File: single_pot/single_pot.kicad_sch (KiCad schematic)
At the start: 4 parts, among them J1 I/O connector

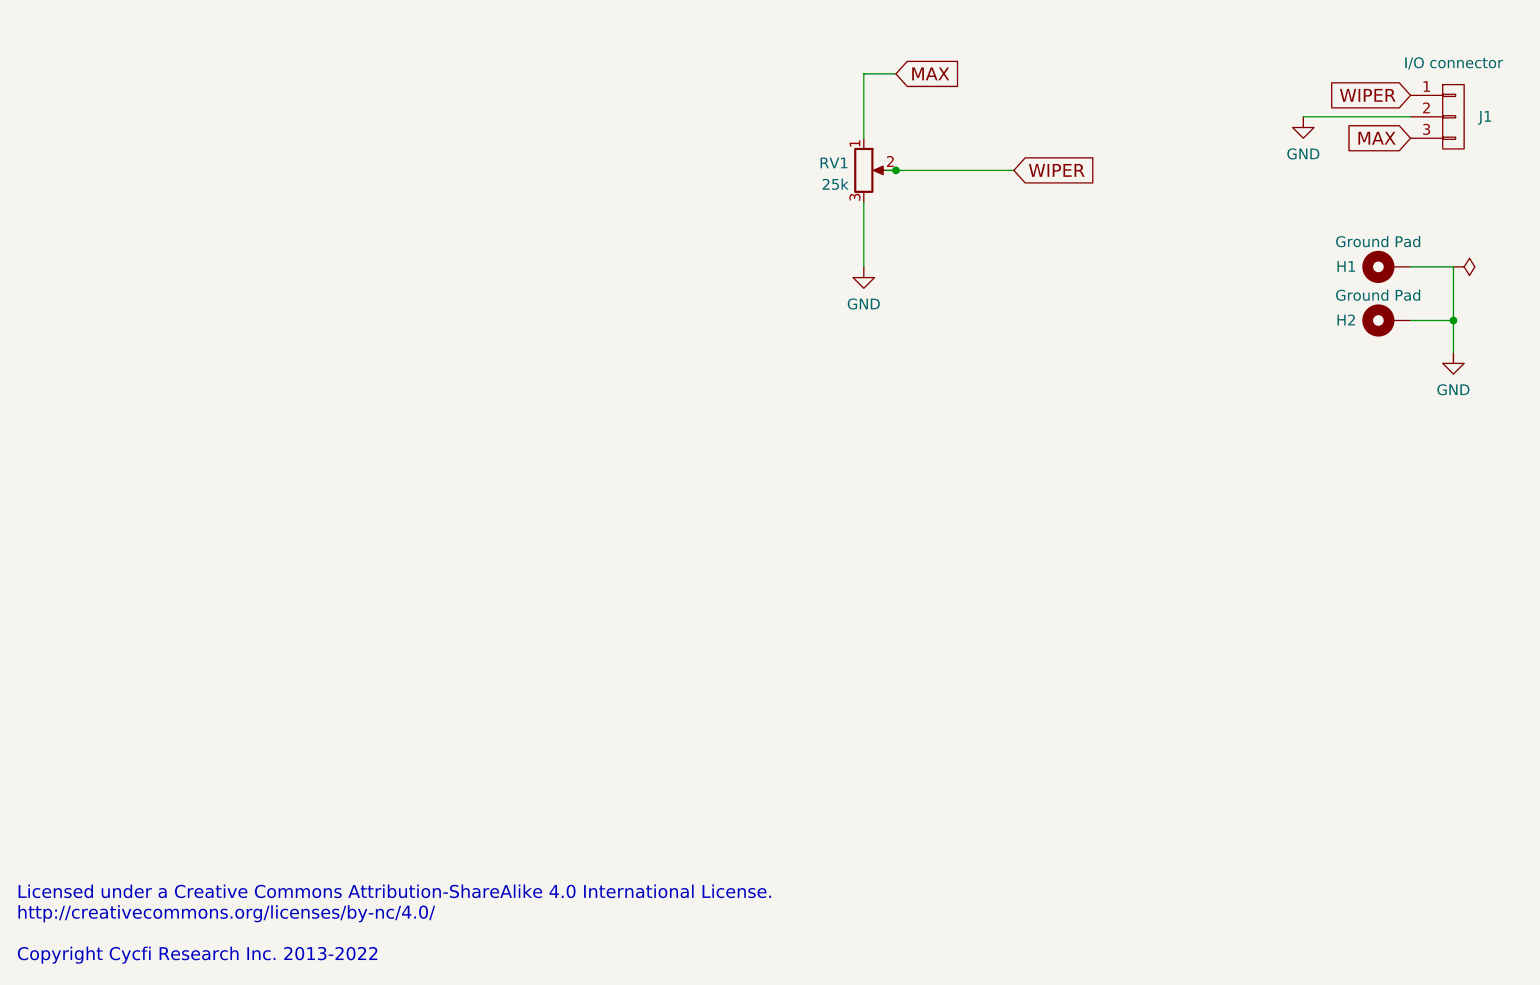
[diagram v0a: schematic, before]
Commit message: Added taper resistor
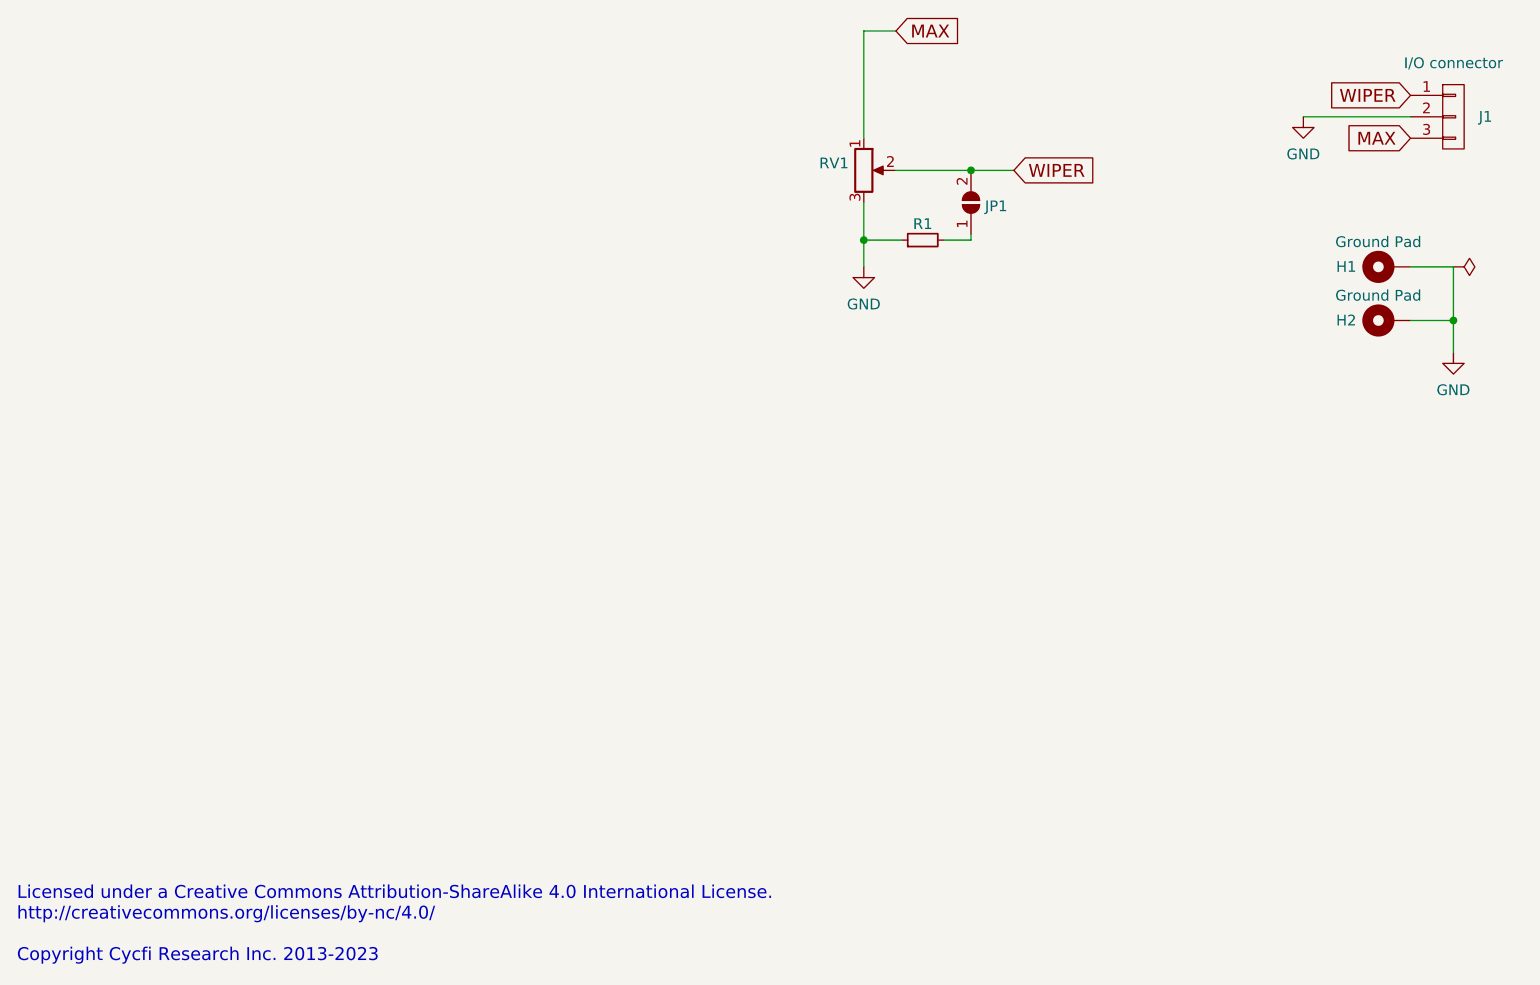
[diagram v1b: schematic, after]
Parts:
- added JP1: SolderJumper_2_Open, Jumper:SolderJumper-2_P1.3mm_Open_TrianglePad1.0x1.5mm, symbol Jumper:SolderJumper_2_Open
- added R1: 4.7k, Resistor_SMD:R_0805_2012Metric_Pad1.20x1.40mm_HandSolder, symbol Device:R_Small
- RV1: value 25k -> 500k
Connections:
- net GND: now also R1.1
- net WIPER: now also JP1.2 (B)
- new net: JP1.1 (A), R1.2
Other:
- note added: "Licensed under a Creative Commons Attribution-ShareAlike 4.0 International License. http://creativecommons.org/licenses/by-nc/4.0/ Copyright Cycfi Research Inc. 2013-2023"
- note removed: "Licensed under a Creative Commons Attribution-ShareAlike 4.0 International License. http://creativecommons.org/licenses/by-nc/4.0/ Copyright Cycfi Research Inc. 2013-2022"
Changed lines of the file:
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@@
   (title_block
     (title "CV Pot Big")
-    (date "2022-04-20")
-    (rev "v3.0")
+    (date "2023-08-05")
+    (rev "v3.1")
     (company "Document Number: 2022005")
   )
   (junction (at 194.31 111.76) (diameter 0) (color 0 0 0 0)
   )
-  (junction (at 128.27 93.98) (diameter 0) (color 0 0 0 0)
+  (junction (at 137.16 93.98) (diameter 0) (color 0 0 0 0)
+  )
+  (junction (at 124.46 102.235) (diameter 0) (color 0 0 0 0)
   )
   (wire (pts (xy 189.23 105.41) (xy 194.31 105.41))
@@
     (stroke (width 0) (type default) (color 0 0 0 0))
   )
-  (wire (pts (xy 124.46 97.79) (xy 124.46 105.41))
-    (stroke (width 0) (type default) (color 0 0 0 0))
-  )
-  (wire (pts (xy 128.27 82.55) (xy 124.46 82.55))
+  (wire (pts (xy 124.46 97.79) (xy 124.46 102.235))
+    (stroke (width 0) (type default) (color 0 0 0 0))
+  )
+  (wire (pts (xy 137.16 102.235) (xy 133.985 102.235))
+    (stroke (width 0) (type default) (color 0 0 0 0))
+  )
+  (wire (pts (xy 137.16 93.98) (xy 142.24 93.98))
+    (stroke (width 0) (type default) (color 0 0 0 0))
+  )
+  (wire (pts (xy 128.27 77.47) (xy 124.46 77.47))
+    (stroke (width 0) (type default) (color 0 0 0 0))
+  )
+  (wire (pts (xy 137.16 101.6) (xy 137.16 102.235))
     (stroke (width 0) (type default) (color 0 0 0 0))
   )
@@
     (stroke (width 0) (type default) (color 0 0 0 0))
   )
-  (wire (pts (xy 128.27 93.98) (xy 142.24 93.98))
-    (stroke (width 0) (type default) (color 0 0 0 0))
-  )
-  (wire (pts (xy 124.46 82.55) (xy 124.46 90.17))
+  (wire (pts (xy 124.46 77.47) (xy 124.46 90.17))
+    (stroke (width 0) (type default) (color 0 0 0 0))
+  )
+  (wire (pts (xy 128.27 93.98) (xy 137.16 93.98))
     (stroke (width 0) (type default) (color 0 0 0 0))
   )
@@
     (stroke (width 0) (type default) (color 0 0 0 0))
   )
-  (wire (pts (xy 127 93.98) (xy 128.27 93.98))
-    (stroke (width 0) (type default) (color 0 0 0 0))
-  )
-  (text "Licensed under a Creative Commons Attribution-ShareAlike 4.0 International License. \nhttp://creativecommons.org/licenses/by-nc/4.0/\n\nCopyright Cycfi Research Inc. 2013-2022"
+  (wire (pts (xy 124.46 102.235) (xy 124.46 105.41))
+    (stroke (width 0) (type default) (color 0 0 0 0))
+  )
+  (wire (pts (xy 124.46 102.235) (xy 128.905 102.235))
+    (stroke (width 0) (type default) (color 0 0 0 0))
+  )
+  (text "Licensed under a Creative Commons Attribution-ShareAlike 4.0 International License. \nhttp://creativecommons.org/licenses/by-nc/4.0/\n\nCopyright Cycfi Research Inc. 2013-2023"
     (at 24.13 187.96 0)
     (effects (font (size 1.524 1.524)) (justify left bottom))
@@
     )
   )
-  (global_label "MAX" (shape input) (at 128.27 82.55 0) (fields_autoplaced)
+  (global_label "MAX" (shape input) (at 128.27 77.47 0) (fields_autoplaced)
     (effects (font (size 1.524 1.524)) (justify left))
-    (property "Intersheet References" "${INTERSHEET_REFS}" (id 0) (at 135.5583 82.4548 0)
+    (property "Intersheet References" "${INTERSHEET_REFS}" (id 0) (at 135.5583 77.3748 0)
       (effects (font (size 1.524 1.524)) (justify left) hide)
     )
@@
     )
   )
+  (symbol (lib_id "Jumper:SolderJumper_2_Open") (at 137.16 97.79 90) (unit 1)
+    (in_bom yes) (on_board yes) (fields_autoplaced)
+    (property "Reference" "JP1" (id 0) (at 138.811 98.2238 90)
+      (effects (font (size 1.27 1.27)) (justify right))
+    )
+    (property "Value" "SolderJumper_2_Open" (id 1) (at 135.1081 97.79 0)
+      (effects (font (size 1.27 1.27)) hide)
+    )
+    (property "Footprint" "Jumper:SolderJumper-2_P1.3mm_Open_TrianglePad1.0x1.5mm" (id 2) (at 137.16 97.79 0)
+      (effects (font (size 1.27 1.27)) hide)
+    )
+    (property "Datasheet" "~" (id 3) (at 137.16 97.79 0)
+      (effects (font (size 1.27 1.27)) hide)
+    )
+    (pin "1")
+    (pin "2")
+  )
   (symbol (lib_id "power:GND") (at 176.53 87.63 0) (unit 1)
     (in_bom yes) (on_board yes) (fields_autoplaced)
@@
       (effects (font (size 1.27 1.27)) (justify right))
     )
-    (property "Value" "25k" (id 1) (at 122.6821 95.6822 0)
-      (effects (font (size 1.27 1.27)) (justify right))
+    (property "Value" "500k" (id 1) (at 122.6821 95.6822 0)
+      (effects (font (size 1.27 1.27)) (justify right) hide)
     )
     (property "Footprint" "cycfi_library:bourns_pdb241" (id 2) (at 124.46 93.98 0)
@@
     (pin "2")
     (pin "3")
+  )
+  (symbol (lib_id "Device:R_Small") (at 131.445 102.235 90) (unit 1)
+    (in_bom yes) (on_board yes) (fields_autoplaced)
+    (property "Reference" "R1" (id 0) (at 131.445 100.3356 90))
+    (property "Value" "4.7k" (id 1) (at 133.1472 100.7364 0)
+      (effects (font (size 1.27 1.27)) (justify left) hide)
+    )
+    (property "Footprint" "Resistor_SMD:R_0805_2012Metric_Pad1.20x1.40mm_HandSolder" (id 2) (at 131.445 102.235 0)
+      (effects (font (size 1.27 1.27)) hide)
+    )
+    (property "Datasheet" "~" (id 3) (at 131.445 102.235 0)
+      (effects (font (size 1.27 1.27)) hide)
+    )
+    (pin "1")
+    (pin "2")
   )
   (symbol (lib_id "Mechanical:MountingHole_Pad") (at 186.69 105.41 90) (unit 1)
@@
       (reference "J1") (unit 1) (value "I/O connector") (footprint "cycfi_library:pin_header_1x3p_2.54mm_smd_horizontal")
     )
+    (path "/23fec8ed-cfa2-45d5-ad2e-d596df70e7f8"
+      (reference "JP1") (unit 1) (value "SolderJumper_2_Open") (footprint "Jumper:SolderJumper-2_P1.3mm_Open_TrianglePad1.0x1.5mm")
+    )
+    (path "/9c599602-3e33-4423-8cbd-18a49d3426b4"
+      (reference "R1") (unit 1) (value "4.7k") (footprint "Resistor_SMD:R_0805_2012Metric_Pad1.20x1.40mm_HandSolder")
+    )
     (path "/9763309a-c9ed-492f-a4a9-0b6f407725b0"
-      (reference "RV1") (unit 1) (value "25k") (footprint "cycfi_library:bourns_pdb241")
-    )
-  )
+      (reference "RV1") (unit 1) (value "500k") (footprint "cycfi_library:bourns_pdb241")
+    )
+  )

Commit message: Update to v3.1
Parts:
- R1: value 4.7k -> 100k; LCSC (none) -> C149504
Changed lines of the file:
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@@
     (in_bom yes) (on_board yes) (fields_autoplaced)
     (property "Reference" "R1" (id 0) (at 131.445 100.3356 90))
-    (property "Value" "4.7k" (id 1) (at 133.1472 100.7364 0)
+    (property "Value" "100k" (id 1) (at 133.1472 100.7364 0)
       (effects (font (size 1.27 1.27)) (justify left) hide)
     )
@@
     (property "Datasheet" "~" (id 3) (at 131.445 102.235 0)
       (effects (font (size 1.27 1.27)) hide)
+    )
+    (property "LCSC" "C149504" (id 4) (at 131.445 102.235 90)
+      (effects (font (size 1.524 1.524)) hide)
     )
     (pin "1")
@@
     )
     (path "/9c599602-3e33-4423-8cbd-18a49d3426b4"
-      (reference "R1") (unit 1) (value "4.7k") (footprint "Resistor_SMD:R_0805_2012Metric_Pad1.20x1.40mm_HandSolder")
+      (reference "R1") (unit 1) (value "100k") (footprint "Resistor_SMD:R_0805_2012Metric_Pad1.20x1.40mm_HandSolder")
     )
     (path "/9763309a-c9ed-492f-a4a9-0b6f407725b0"
